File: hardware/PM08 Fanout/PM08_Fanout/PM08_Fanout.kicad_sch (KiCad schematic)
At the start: 1 part, among them J1 IDC Connector

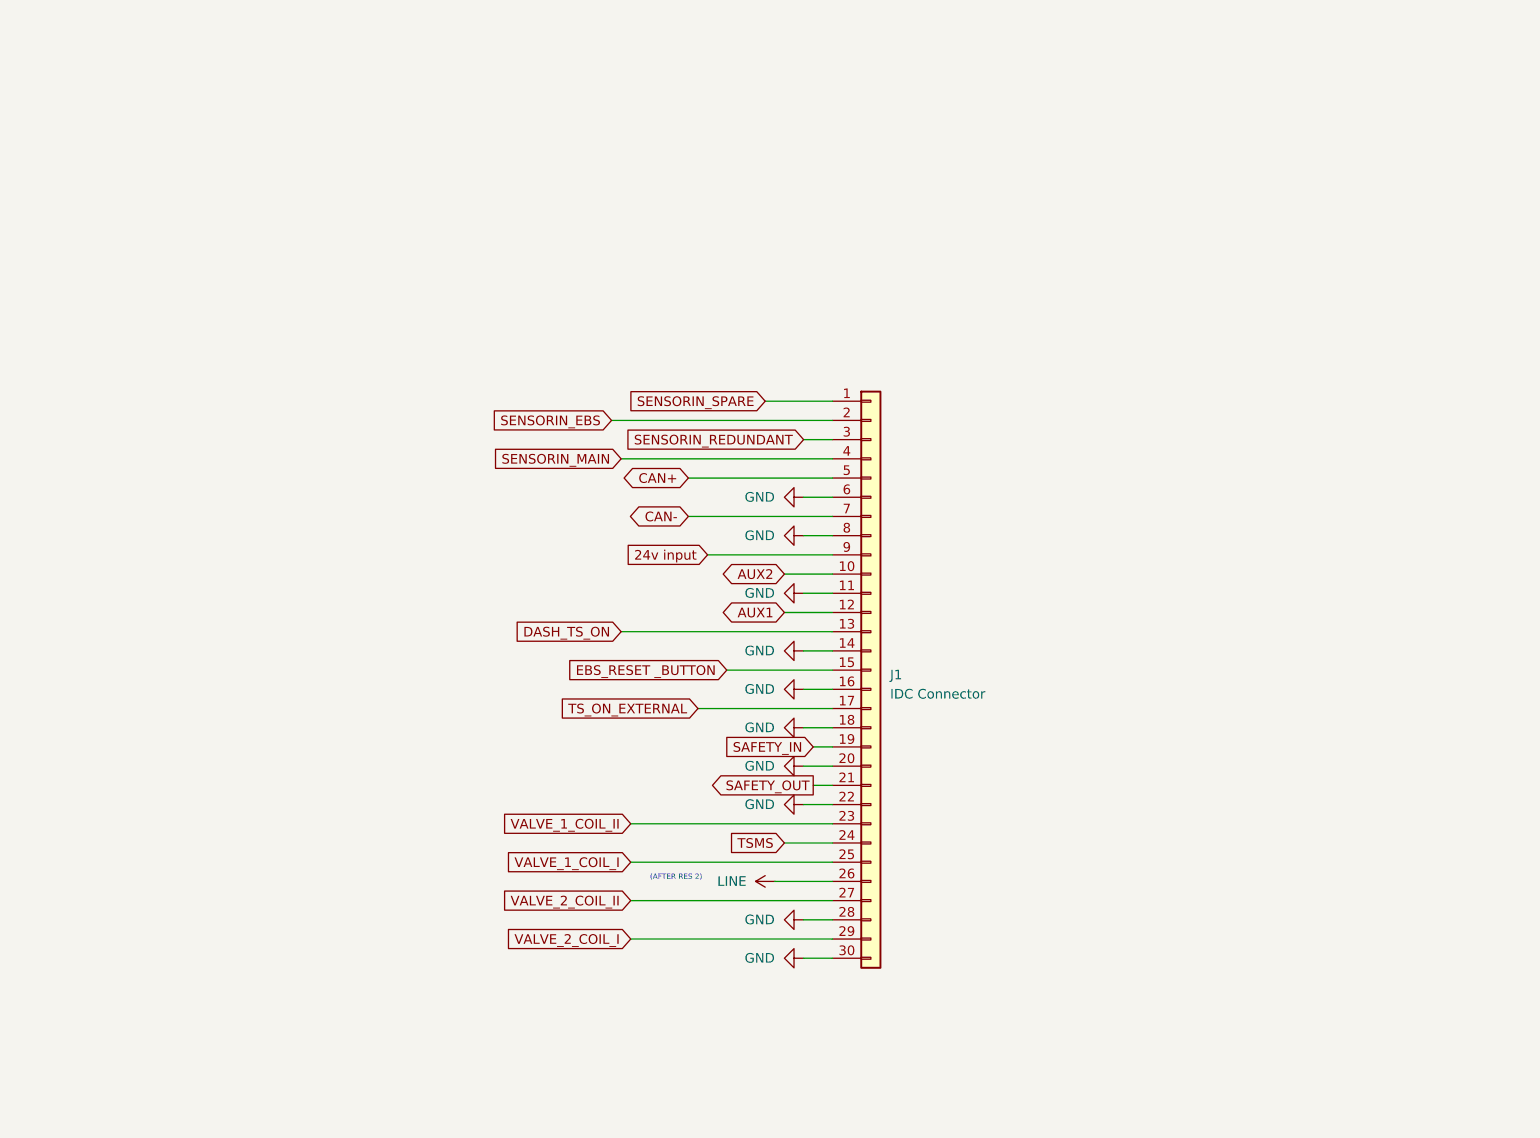
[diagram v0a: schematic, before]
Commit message: Added PM08 connector board
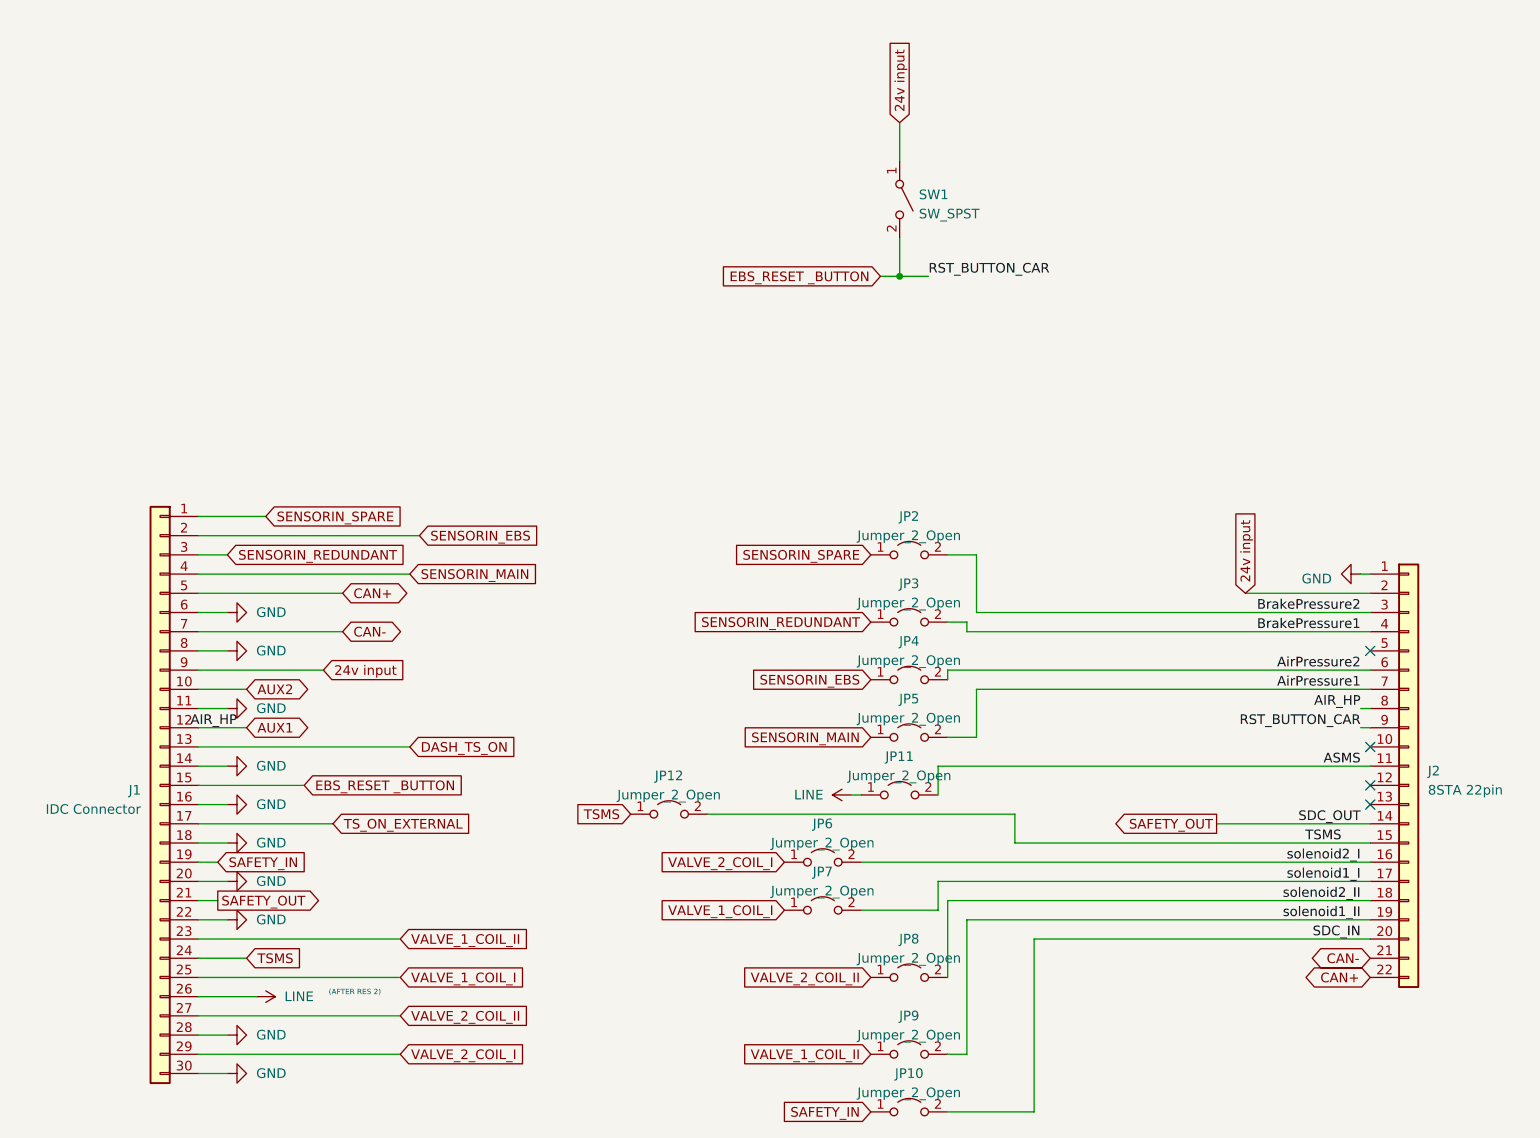
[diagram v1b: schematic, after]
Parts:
- added J2: 8STA 22pin, LocalLibrary:AS612-35PN, symbol Connector_Generic:Conn_01x22
- added JP10, JP11, JP12, JP2, JP3, JP4, JP5, JP6, JP7, JP8, JP9: Jumper_2_Open, Connector_PinHeader_2.54mm:PinHeader_1x02_P2.54mm_Vertical, symbol Jumper:Jumper_2_Open
- added SW1: SW_SPST, Button_Switch_THT:SW_PUSH_6mm, symbol Switch:SW_SPST
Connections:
- net 24v input: now also J2.2 (Pin_2), SW1.1 (A)
- net AUX1: now also J2.8 (Pin_8)
- net CAN+: now also J2.22 (Pin_22)
- net CAN-: now also J2.21 (Pin_21)
- net EBS_RESET _BUTTON: now also J2.9 (Pin_9), SW1.2 (B)
- net GND: now also J2.1 (Pin_1)
- net LINE: now also JP11.1 (A)
- net SAFETY_IN: now also JP10.1 (A)
- net SAFETY_OUT: now also J2.14 (Pin_14)
- net SENSORIN_EBS: now also JP4.1 (A)
- net SENSORIN_MAIN: now also JP5.1 (A)
- net SENSORIN_REDUNDANT: now also JP3.1 (A)
- net SENSORIN_SPARE: now also JP2.1 (A)
- net TSMS: now also J2.15 (Pin_15), JP12.1 (A), JP12.2 (B)
- net VALVE_1_COIL_I: now also JP7.1 (A)
- net VALVE_1_COIL_II: now also JP9.1 (A)
- net VALVE_2_COIL_I: now also JP6.1 (A)
- net VALVE_2_COIL_II: now also JP8.1 (A)
- new net ASMS: J2.11 (Pin_11), JP11.2 (B)
- new net AirPressure1: J2.7 (Pin_7), JP5.2 (B)
- new net AirPressure2: J2.6 (Pin_6), JP4.2 (B)
- new net BrakePressure1: J2.4 (Pin_4), JP3.2 (B)
- new net BrakePressure2: J2.3 (Pin_3), JP2.2 (B)
- new net SDC_IN: J2.20 (Pin_20), JP10.2 (B)
- new net solenoid1_I: J2.17 (Pin_17), JP7.2 (B)
- new net solenoid1_II: J2.19 (Pin_19), JP9.2 (B)
- new net solenoid2_I: J2.16 (Pin_16), JP6.2 (B)
- new net solenoid2_II: J2.18 (Pin_18), JP8.2 (B)
- no-connect marks 0 -> 4
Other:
- moved on the sheet: J1
